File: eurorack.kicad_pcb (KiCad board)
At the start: 2 copper layers, 84.7 x 30 mm, 18 parts, among them J1 Eurorack 10-pin power, J10 display socket, J2 to carrier row A (female 8.5m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, J3 to carrier row B (female 8.5m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, J4 to hat, above J2 (male), J5 to hat, above J3 (male), J6 (input) IN 3.5mm mono, J7 (output) OUT 3.5mm mono, J8 mates hat J7 (or wires to hat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, U1 K7805-1000R3

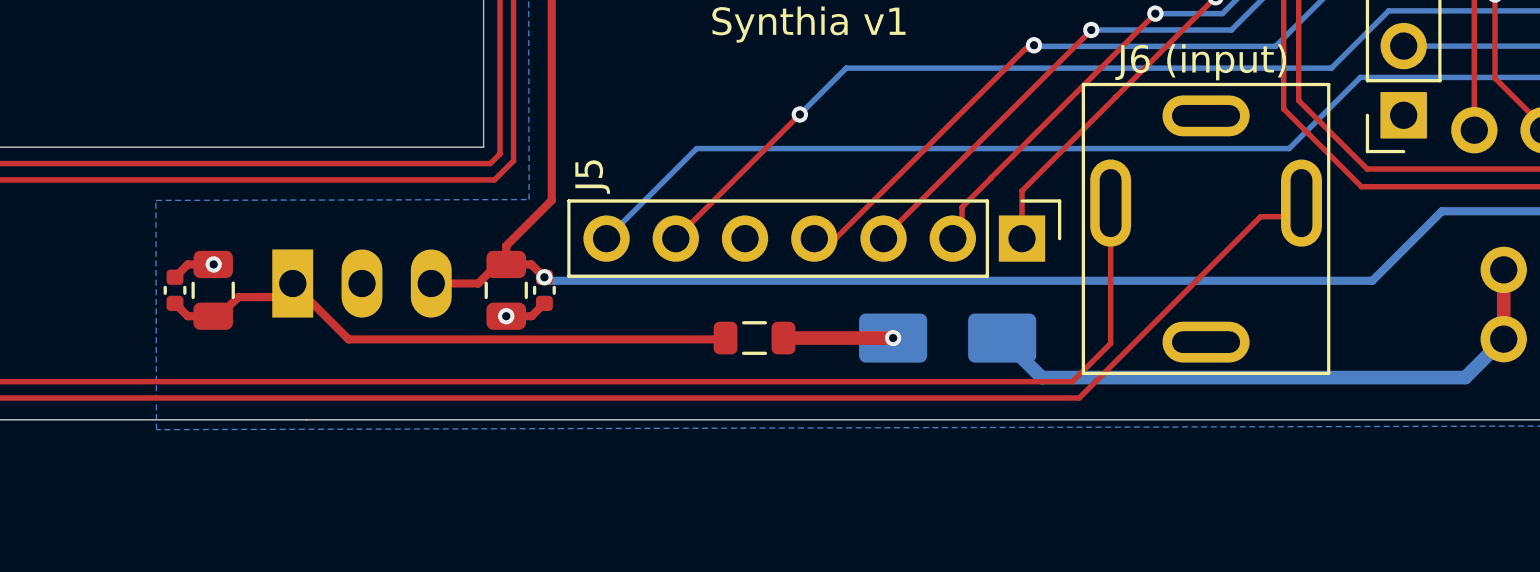
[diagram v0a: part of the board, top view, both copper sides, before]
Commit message: pcb: +5V touch-up; regen fab + docs
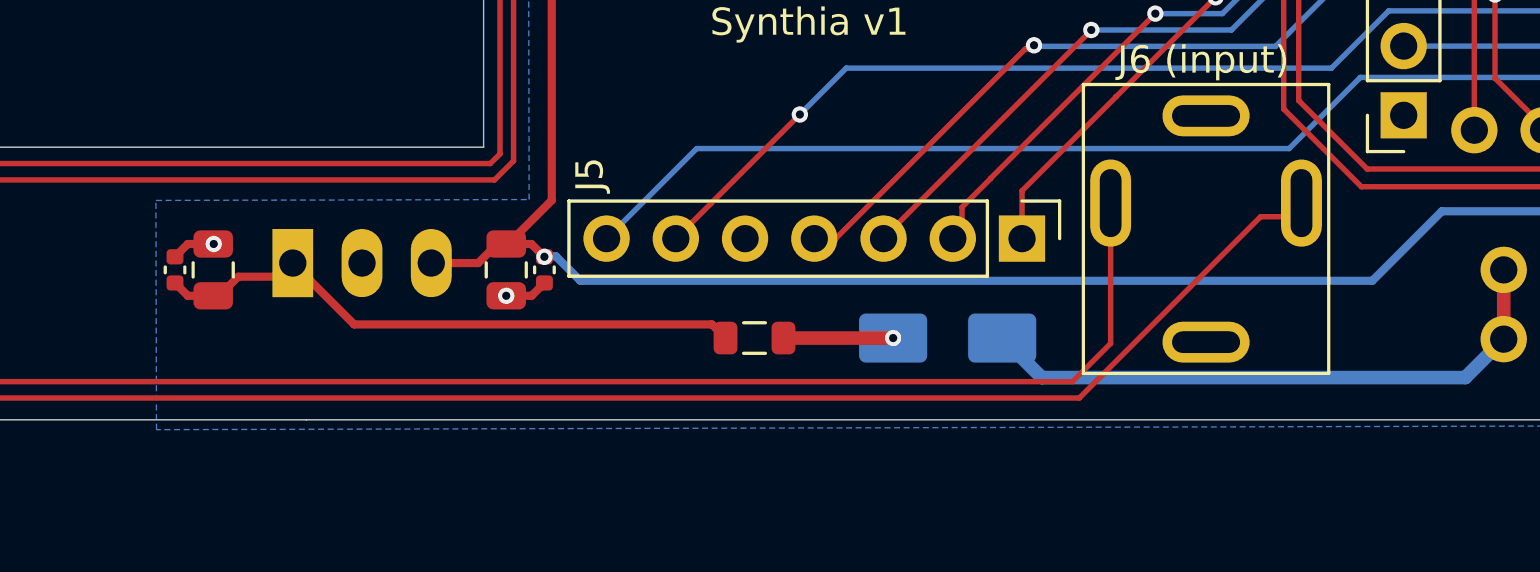
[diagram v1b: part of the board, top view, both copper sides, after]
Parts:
- moved C1 0.75 mm to (86.6, 65.5)
- moved C2 0.75 mm to (85.2, 65.5)
- moved C3 0.75 mm to (97.3, 65.5)
- moved C4 0.75 mm to (98.7, 65.5)
- moved U1 0.75 mm to (89.5, 65.2)
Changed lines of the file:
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@@
 	(footprint "Capacitor_SMD:C_0402_1005Metric"
 		(layer "F.Cu")
-		(at 85.18 66.25 90)
+		(at 85.18 65.5 90)
 		(descr "Capacitor SMD 0402 (1005 Metric), square (rectangular) end terminal, IPC-7351 nominal, (Body size source: IPC-SM-782 page 76, https://www.pcb-3d.com/wordpress/wp-content/uploads/ipc-sm-782a_amendment_1_and_2.pdf)")
 		(tags "capacitor")
@@
 	(footprint "Capacitor_SMD:C_0805_2012Metric"
 		(layer "F.Cu")
-		(at 97.33 66.25 -90)
+		(at 97.33 65.5 -90)
 		(descr "Capacitor SMD 0805 (2012 Metric), square (rectangular) end terminal, IPC-7351 nominal, (Body size source: IPC-SM-782 page 76, https://www.pcb-3d.com/wordpress/wp-content/uploads/ipc-sm-782a_amendment_1_and_2.pdf, https://docs.google.com/spreadsheets/d/1BsfQQcO9C6DZCsRaXUlFlo91Tg2WpOkGARC1WS5S8t0/edit?usp=sharing)")
 		(tags "capacitor")
@@
 	(footprint "Capacitor_SMD:C_0402_1005Metric"
 		(layer "F.Cu")
-		(at 98.73 66.25 -90)
+		(at 98.73 65.5 -90)
 		(descr "Capacitor SMD 0402 (1005 Metric), square (rectangular) end terminal, IPC-7351 nominal, (Body size source: IPC-SM-782 page 76, https://www.pcb-3d.com/wordpress/wp-content/uploads/ipc-sm-782a_amendment_1_and_2.pdf)")
 		(tags "capacitor")
@@
 	(footprint "Capacitor_SMD:C_0805_2012Metric"
 		(layer "F.Cu")
-		(at 86.58 66.25 90)
+		(at 86.58 65.5 90)
 		(descr "Capacitor SMD 0805 (2012 Metric), square (rectangular) end terminal, IPC-7351 nominal, (Body size source: IPC-SM-782 page 76, https://www.pcb-3d.com/wordpress/wp-content/uploads/ipc-sm-782a_amendment_1_and_2.pdf, https://docs.google.com/spreadsheets/d/1BsfQQcO9C6DZCsRaXUlFlo91Tg2WpOkGARC1WS5S8t0/edit?usp=sharing)")
 		(tags "capacitor")
@@
 	(footprint "Converter_DCDC:Converter_DCDC_TRACO_TSR-1_THT"
 		(layer "B.Cu")
-		(at 89.5 66)
+		(at 89.5 65.25)
 		(descr "DCDC-Converter, TRACO, TSR 1-xxxx")
 		(tags "DCDC-Converter TRACO TSR-1")
@@
 	)
 	(segment
-		(start 86.58 67.2)
-		(end 85.65 67.2)
+		(start 86.58 66.45)
+		(end 85.65 66.45)
 		(width 0.3)
 		(layer "F.Cu")
@@
 	)
 	(segment
-		(start 91.55 68.05)
-		(end 105.325 68.05)
+		(start 104.875 67.5)
+		(end 91.75 67.5)
 		(width 0.3)
 		(layer "F.Cu")
@@
 	)
 	(segment
-		(start 89 66.5)
-		(end 89.5 66)
+		(start 91.75 67.5)
+		(end 89.5 65.25)
 		(width 0.3)
 		(layer "F.Cu")
@@
 	)
 	(segment
-		(start 105.325 68.05)
-		(end 105.375 68)
+		(start 89 65.75)
+		(end 89.5 65.25)
 		(width 0.3)
 		(layer "F.Cu")
@@
 	)
 	(segment
-		(start 86.58 67.2)
-		(end 86.8 67.2)
+		(start 86.58 66.45)
+		(end 86.8 66.45)
 		(width 0.3)
 		(layer "F.Cu")
@@
 	)
 	(segment
-		(start 86.8 67.2)
-		(end 87.5 66.5)
+		(start 86.8 66.45)
+		(end 87.5 65.75)
 		(width 0.3)
 		(layer "F.Cu")
@@
 	)
 	(segment
-		(start 89.5 66)
-		(end 91.55 68.05)
+		(start 105.375 68)
+		(end 104.875 67.5)
 		(width 0.3)
 		(layer "F.Cu")
@@
 	)
 	(segment
-		(start 85.65 67.2)
-		(end 85.18 66.73)
+		(start 85.65 66.45)
+		(end 85.18 65.98)
 		(width 0.3)
 		(layer "F.Cu")
@@
 	)
 	(segment
-		(start 87.5 66.5)
-		(end 89 66.5)
+		(start 87.5 65.75)
+		(end 89 65.75)
 		(width 0.3)
 		(layer "F.Cu")
@@
 	)
 	(segment
-		(start 85.65 65.3)
-		(end 86.58 65.3)
+		(start 85.65 64.55)
+		(end 86.58 64.55)
 		(width 0.3)
 		(layer "F.Cu")
@@
 	)
 	(segment
-		(start 97.33 67.2)
-		(end 98.26 67.2)
+		(start 97.33 66.45)
+		(end 98.26 66.45)
 		(width 0.3)
 		(layer "F.Cu")
@@
 	)
 	(segment
-		(start 85.18 65.77)
-		(end 85.65 65.3)
+		(start 85.18 65.02)
+		(end 85.65 64.55)
 		(width 0.3)
 		(layer "F.Cu")
@@
 	)
 	(segment
-		(start 86.58 65.3)
-		(end 86.6 65.3)
+		(start 86.58 64.55)
+		(end 86.6 64.55)
 		(width 0.2)
 		(layer "F.Cu")
@@
 	)
 	(segment
-		(start 98.26 67.2)
-		(end 98.73 66.73)
+		(start 98.26 66.45)
+		(end 98.73 65.98)
 		(width 0.3)
 		(layer "F.Cu")
@@
 	)
 	(via
-		(at 86.6 65.3)
+		(at 86.6 64.55)
 		(size 0.6)
 		(drill 0.3)
@@
 	)
 	(via
-		(at 97.33 67.2)
+		(at 97.33 66.45)
 		(size 0.6)
 		(drill 0.3)
@@
 	)
 	(segment
-		(start 96.3 66)
-		(end 94.58 66)
+		(start 96.3 65.25)
+		(end 94.58 65.25)
 		(width 0.3)
 		(layer "F.Cu")
@@
 	)
 	(segment
-		(start 98.73 65.77)
-		(end 98.72 65.77)
+		(start 98.73 65.02)
+		(end 98.72 65.02)
 		(width 0.2)
 		(layer "F.Cu")
@@
 	)
 	(segment
-		(start 97.33 65.3)
-		(end 97 65.3)
+		(start 97.33 64.55)
+		(end 97 64.55)
 		(width 0.3)
 		(layer "F.Cu")
@@
 	)
 	(segment
-		(start 98.25 65.3)
-		(end 97.33 65.3)
+		(start 98.25 64.55)
+		(end 97.33 64.55)
 		(width 0.3)
 		(layer "F.Cu")
@@
 	)
 	(segment
-		(start 98.72 65.77)
-		(end 98.25 65.3)
+		(start 98.72 65.02)
+		(end 98.25 64.55)
 		(width 0.3)
 		(layer "F.Cu")
@@
 	)
 	(segment
-		(start 97.33 64.62)
-		(end 97.33 65.3)
-		(width 0.3)
-		(layer "F.Cu")
-		(net "+5V")
-	)
-	(segment
-		(start 97 65.3)
-		(end 96.3 66)
+		(start 97 64.55)
+		(end 96.3 65.25)
 		(width 0.3)
 		(layer "F.Cu")
@@
 	)
 	(via
-		(at 98.73 65.77)
+		(at 98.73 65.02)
 		(size 0.6)
 		(drill 0.3)
@@
 	)
 	(segment
+		(start 99.15 65)
+		(end 98.84 65)
+		(width 0.3)
+		(layer "B.Cu")
+		(net "+5V")
+	)
+	(segment
+		(start 98.82 65.02)
+		(end 98.73 65.02)
+		(width 0.3)
+		(layer "B.Cu")
+		(net "+5V")
+	)
+	(segment
+		(start 98.86 65.15)
+		(end 98.73 65.02)
+		(width 0.3)
+		(layer "B.Cu")
+		(net "+5V")
+	)
+	(segment
+		(start 129.1 65.9)
+		(end 100.05 65.9)
+		(width 0.3)
+		(layer "B.Cu")
+		(net "+5V")
+	)
+	(segment
 		(start 145.87 63.35)
 		(end 131.65 63.35)
@@
 	)
 	(segment
-		(start 129.1 65.9)
-		(end 98.86 65.9)
+		(start 100.05 65.9)
+		(end 99.15 65)
 		(width 0.3)
 		(layer "B.Cu")
@@
 	)
 	(segment
-		(start 98.86 65.9)
-		(end 98.73 65.77)
+		(start 98.84 65)
+		(end 98.82 65.02)
 		(width 0.3)
 		(layer "B.Cu")

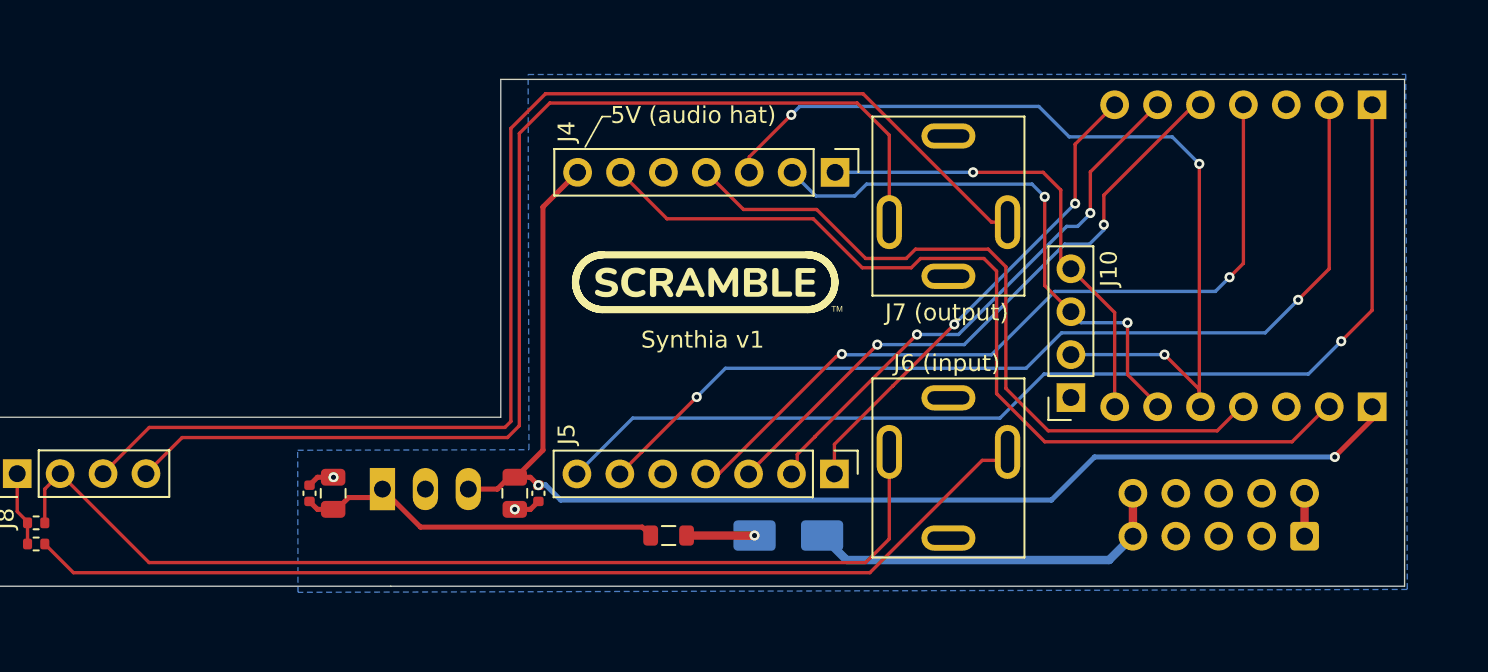
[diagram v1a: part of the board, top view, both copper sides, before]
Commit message: sch+pcb: eurorack I/O stage — input pad 100k/39k, TL072 x4.9 output amp on ±12V
- input divider now populated (R2/R3 = 100k/39k, -11.5dB): ±5V modular
  swings land inside the hat codec range; also protects against CV/gate
  mis-patches. Guitar-level alternative (R2=0R, R3 off) documented
- output: TL072 (C6961) x4.9 on +12V_F and a newly conditioned -12V rail
  (D2 SS34 + FB2 bead + 100n/22u), hat ~2Vpp -> ~10Vpp modular level,
  1k series out; spare half terminated; AOUT_S bonded to GND at one
  point (NT1 net tie); PWR_FLAG on -12V_F
- all new parts placed + routed, DRC clean; audit: no aggressors near
  the input pair, amp output >=3mm from input path everywhere
- fp-lib-table: add Package_SO + NetTie; BOM: 3 new lines (all LCSC
  in-stock verified), R2/R7 and R3/R5 share parts; ~45c/board added
- fab regen (CPL 19 placements, no DNP); verify D1/D2/U2 rotations in
  JLC preview; doc PDFs + STEP regenerated
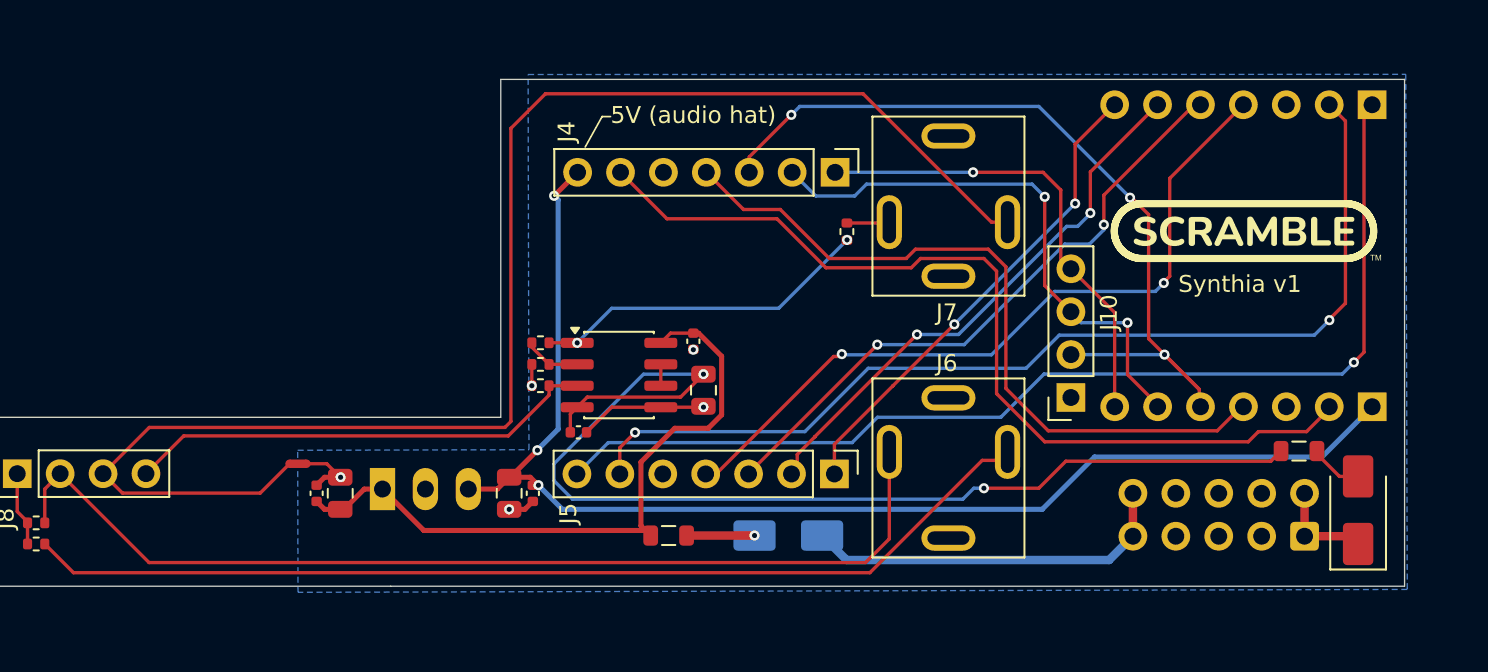
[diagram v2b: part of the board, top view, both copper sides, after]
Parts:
- added C5: 100nF, Capacitor_SMD:C_0402_1005Metric, F.Cu at (107.9, 56.5)
- added C6: 100nF, Capacitor_SMD:C_0402_1005Metric, F.Cu at (101.1, 61.9)
- added C7: 22uF 25V, Capacitor_SMD:C_0805_2012Metric, F.Cu at (108.5, 59.4)
- added D2: SS34, Diode_SMD:D_SMA, F.Cu at (147.2, 66.5)
- added FB2: 600R@100MHz, Inductor_SMD:L_0805_2012Metric, F.Cu at (143.8, 63.0)
- added NT1: NetTie_2, NetTie:NetTie-2_SMD_Pad0.5mm, F.Cu at (84.5, 63.8)
- added R4: 10k, Resistor_SMD:R_0402_1005Metric, F.Cu at (98.8, 57.9)
- added R5: 39k, Resistor_SMD:R_0402_1005Metric, F.Cu at (98.8, 56.6)
- added R6: 1k, Resistor_SMD:R_0402_1005Metric, F.Cu at (117.0, 50.0)
- added R7: 100k, Resistor_SMD:R_0402_1005Metric, F.Cu at (98.8, 59.1)
- added U2: TL072, Package_SO:SOIC-8_3.9x4.9mm_P1.27mm, F.Cu at (103.5, 58.5)
- J6: renamed from J6 (input)
- J7: renamed from J7 (output)
- R2: value 0R -> 100k
- R3: value DNP -> 39k
- moved C1 0.42 mm to (87.0, 65.5)
- moved C2 0.42 mm to (85.6, 65.5)
- moved C3 0.33 mm to (97.0, 65.5)
- moved C4 0.33 mm to (98.4, 65.5)
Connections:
- J8 pad 4: AOUT_T -> AOUT_HAT
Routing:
- net -12V_F: track 0.00 -> 66.7 mm, vias 0 -> 2
- net AOUT_T: track 69.2 -> 2.53 mm
- net AOUT_HAT: track 0.00 -> 28.0 mm
- net AOUT_AMP: track 0.00 -> 20.2 mm, vias 0 -> 2
- net +12V_F: track 22.0 -> 40.0 mm
- net AOUT_S: track 76.2 -> 88.4 mm
- net GND: track 3.21 -> 14.4 mm, vias 2 -> 5
- net +3V3: track 53.7 -> 49.5 mm
- net LRCK: track 56.7 -> 60.2 mm
- net AOUT_FB: track 0.00 -> 3.37 mm
- net -12V: track 2.54 -> 5.90 mm
- net -12V_P: track 0.00 -> 2.52 mm
- net DSDIN: track 46.4 -> 44.3 mm
- net U2B_FB: track 0.00 -> 1.27 mm
- net ASDOUT: track 63.3 -> 64.4 mm
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
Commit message: sch+pcb: follow hat dual-host pinout — crossover net renames, J10 display taps moved to row-A I2C runs; regen fab + docs; add pinout graphic
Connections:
- J2 pad 1: ASDOUT -> SDA
- J2 pad 2: LRCK -> SCL
- J2 pad 6: MCLK -> LRCK
- J2 pad 7: DET -> ASDOUT
- J3 pad 6: SCL -> MCLK
- J3 pad 7: SDA -> DET
- J4 pad 1: SDA -> DET
- J4 pad 2: SCL -> MCLK
- J5 pad 1: DET -> ASDOUT
- J5 pad 2: MCLK -> LRCK
- J5 pad 6: LRCK -> SCL
- J5 pad 7: ASDOUT -> SDA
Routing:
- net ASDOUT: track 64.4 -> 28.7 mm, vias 1 -> 2
- net SDA: track 27.8 -> 62.2 mm
- net LRCK: track 60.2 -> 32.7 mm
- net SCL: track 32.8 -> 57.8 mm, vias 2 -> 1
- net DSDIN: track 44.3 -> 47.0 mm
- net DET: track 28.7 -> 27.1 mm, vias 2 -> 1
- net MCLK: track 32.7 -> 34.0 mm, vias 2 -> 1
- net +3V3: track 49.5 -> 48.8 mm
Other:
- board text added: "5V (mcu board)"
- board text removed: "5V (ETH board)"
